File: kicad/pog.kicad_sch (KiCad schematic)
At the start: 179 parts, among them P1 USB_C_Plug_USB2.0, U1 ATmega32U4-A

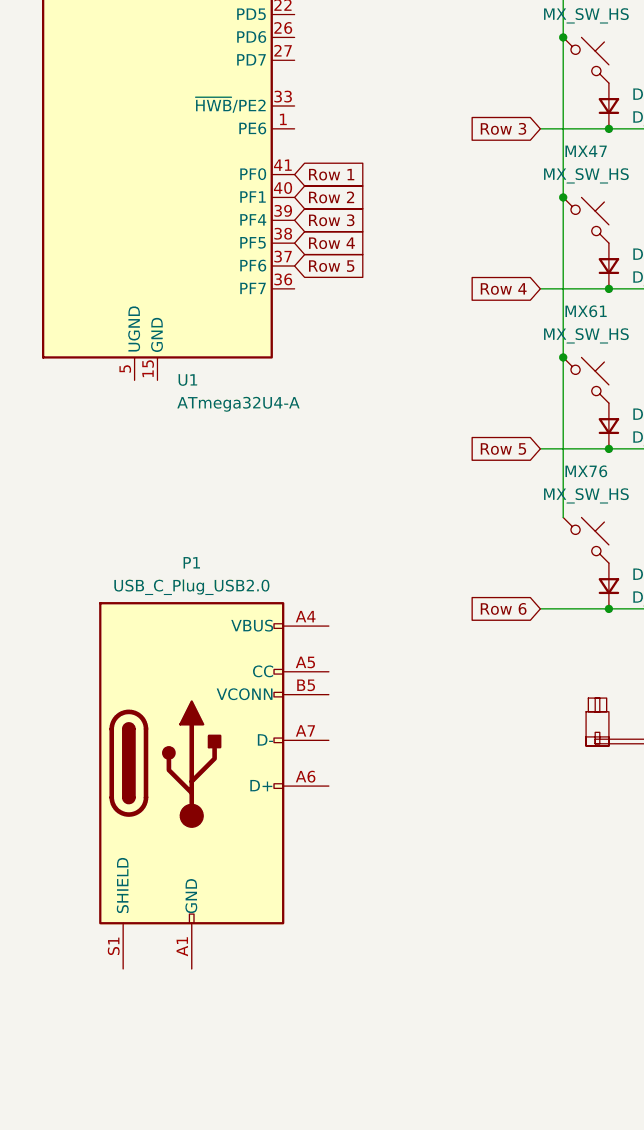
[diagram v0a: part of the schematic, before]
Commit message: more traces and git ignore update
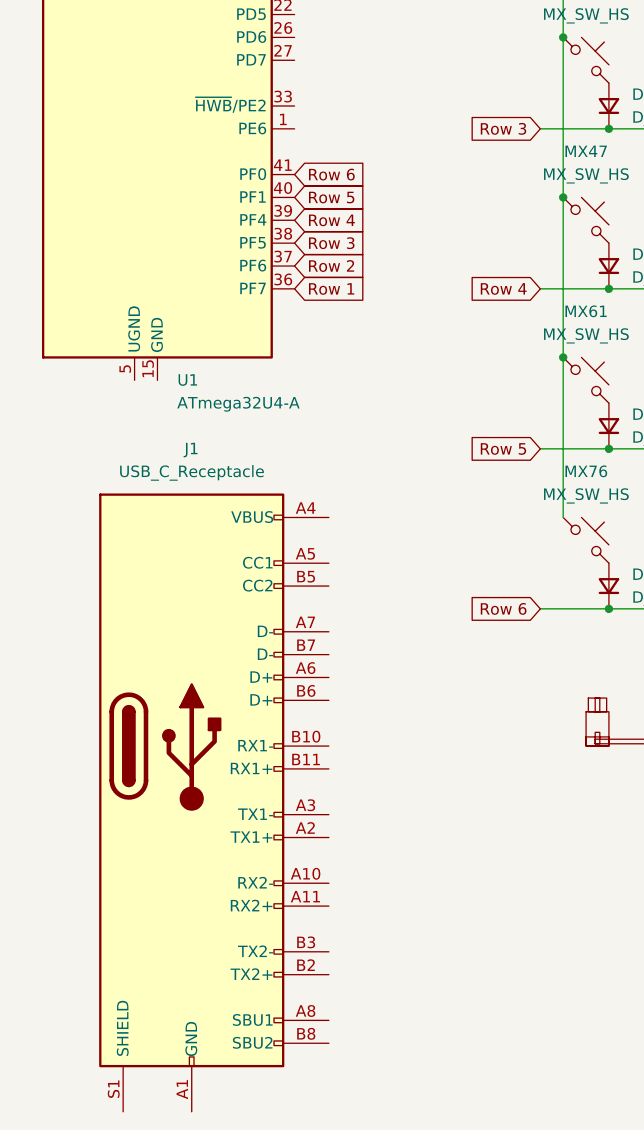
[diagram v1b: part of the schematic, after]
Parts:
- removed P1: USB_C_Plug_USB2.0, Connector_USB:USB_C_Receptacle_HRO_TYPE-C-31-M-12, symbol Connector:USB_C_Plug_USB2.0
- added J1: USB_C_Receptacle, symbol Connector:USB_C_Receptacle
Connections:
- net Row 1: now also U1.36 (PF7); no longer U1.41 (PF0)
- net Row 2: now also U1.37 (PF6); no longer U1.40 (PF1)
- net Row 3: now also U1.38 (PF5); no longer U1.39 (PF4)
- net Row 4: now also U1.39 (PF4); no longer U1.38 (PF5)
- net Row 5: now also U1.40 (PF1); no longer U1.37 (PF6)
- net Row 6: now also U1.41 (PF0)
- new net: J1.A1 (GND), J1.A12 (GND), J1.B1 (GND), J1.B12 (GND)
- new net: J1.A4 (VBUS), J1.A9 (VBUS), J1.B4 (VBUS), J1.B9 (VBUS)
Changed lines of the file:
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@@
     )
   )
-  (global_label "Row 2" (shape input) (at 48.895 87.63 0) (fields_autoplaced)
+  (global_label "Row 2" (shape input) (at 48.895 95.25 0) (fields_autoplaced)
     (effects (font (size 1.27 1.27)) (justify left))
-    (property "Intersheetrefs" "${INTERSHEET_REFS}" (at 57.8068 87.63 0)
+    (property "Intersheetrefs" "${INTERSHEET_REFS}" (at 57.8068 95.25 0)
       (effects (font (size 1.27 1.27)) (justify left) hide)
     )
@@
     )
   )
-  (global_label "Row 5" (shape input) (at 48.895 95.25 0) (fields_autoplaced)
+  (global_label "Row 5" (shape input) (at 48.895 87.63 0) (fields_autoplaced)
     (effects (font (size 1.27 1.27)) (justify left))
-    (property "Intersheetrefs" "${INTERSHEET_REFS}" (at 57.8068 95.25 0)
+    (property "Intersheetrefs" "${INTERSHEET_REFS}" (at 57.8068 87.63 0)
       (effects (font (size 1.27 1.27)) (justify left) hide)
     )
   )
-  (global_label "Row 4" (shape input) (at 48.895 92.71 0) (fields_autoplaced)
+  (global_label "Row 4" (shape input) (at 48.895 90.17 0) (fields_autoplaced)
     (effects (font (size 1.27 1.27)) (justify left))
-    (property "Intersheetrefs" "${INTERSHEET_REFS}" (at 57.8068 92.71 0)
+    (property "Intersheetrefs" "${INTERSHEET_REFS}" (at 57.8068 90.17 0)
+      (effects (font (size 1.27 1.27)) (justify left) hide)
+    )
+  )
+  (global_label "Row 6" (shape input) (at 48.895 85.09 0) (fields_autoplaced)
+    (effects (font (size 1.27 1.27)) (justify left))
+    (property "Intersheetrefs" "${INTERSHEET_REFS}" (at 57.8068 85.09 0)
       (effects (font (size 1.27 1.27)) (justify left) hide)
     )
@@
     )
   )
-  (global_label "Row 1" (shape input) (at 48.895 85.09 0) (fields_autoplaced)
+  (global_label "Row 1" (shape input) (at 48.895 97.79 0) (fields_autoplaced)
     (effects (font (size 1.27 1.27)) (justify left))
-    (property "Intersheetrefs" "${INTERSHEET_REFS}" (at 57.8068 85.09 0)
+    (property "Intersheetrefs" "${INTERSHEET_REFS}" (at 57.8068 97.79 0)
       (effects (font (size 1.27 1.27)) (justify left) hide)
     )
@@
     )
   )
-  (global_label "Row 3" (shape input) (at 48.895 90.17 0) (fields_autoplaced)
+  (global_label "Row 3" (shape input) (at 48.895 92.71 0) (fields_autoplaced)
     (effects (font (size 1.27 1.27)) (justify left))
-    (property "Intersheetrefs" "${INTERSHEET_REFS}" (at 57.8068 90.17 0)
+    (property "Intersheetrefs" "${INTERSHEET_REFS}" (at 57.8068 92.71 0)
       (effects (font (size 1.27 1.27)) (justify left) hide)
     )
@@
     )
   )
-  (symbol (lib_id "Connector:USB_C_Plug_USB2.0") (at 37.465 150.495 0) (unit 1)
-    (in_bom yes) (on_board yes) (dnp no) (fields_autoplaced)
-    (property "Reference" "P1" (at 37.465 128.27 0)
-      (effects (font (size 1.27 1.27)))
-    )
-    (property "Value" "USB_C_Plug_USB2.0" (at 37.465 130.81 0)
-      (effects (font (size 1.27 1.27)))
-    )
-    (property "Footprint" "Connector_USB:USB_C_Receptacle_HRO_TYPE-C-31-M-12" (at 41.275 150.495 0)
-      (effects (font (size 1.27 1.27)) hide)
-    )
-    (property "Datasheet" "https://www.usb.org/sites/default/files/documents/usb_type-c.zip" (at 41.275 150.495 0)
-      (effects (font (size 1.27 1.27)) hide)
-    )
-    (pin "A1")
-    (pin "A12")
-    (pin "A4")
-    (pin "A5")
-    (pin "A6")
-    (pin "A7")
-    (pin "A9")
-    (pin "B1")
-    (pin "B12")
-    (pin "B4")
-    (pin "B5")
-    (pin "B9")
-    (pin "S1")
-    (instances
-      (project "pog"
-        (path "/0904c928-be14-4e09-9349-b8c6153656fb"
-          (reference "P1") (unit 1)
-        )
-      )
-    )
-  )
   (symbol (lib_id "PCM_marbastlib-mx:MX_SW_HS") (at 218.44 72.39 0) (unit 1)
     (in_bom yes) (on_board yes) (dnp no) (fields_autoplaced)
@@
         )
       )
+    )
+  )
+  (symbol (lib_id "Connector:USB_C_Receptacle") (at 37.465 148.59 0) (unit 1)
+    (in_bom yes) (on_board yes) (dnp no) (fields_autoplaced)
+    (property "Reference" "J1" (at 37.465 115.57 0)
+      (effects (font (size 1.27 1.27)))
+    )
+    (property "Value" "USB_C_Receptacle" (at 37.465 118.11 0)
+      (effects (font (size 1.27 1.27)))
+    )
+    (property "Footprint" "" (at 41.275 148.59 0)
+      (effects (font (size 1.27 1.27)) hide)
+    )
+    (property "Datasheet" "https://www.usb.org/sites/default/files/documents/usb_type-c.zip" (at 41.275 148.59 0)
+      (effects (font (size 1.27 1.27)) hide)
+    )
+    (pin "A1")
+    (pin "A10")
+    (pin "A11")
+    (pin "A12")
+    (pin "A2")
+    (pin "A3")
+    (pin "A4")
+    (pin "A5")
+    (pin "A6")
+    (pin "A7")
+    (pin "A8")
+    (pin "A9")
+    (pin "B1")
+    (pin "B10")
+    (pin "B11")
+    (pin "B12")
+    (pin "B2")
+    (pin "B3")
+    (pin "B4")
+    (pin "B5")
+    (pin "B6")
+    (pin "B7")
+    (pin "B8")
+    (pin "B9")
+    (pin "S1")
+    (instances
+      (project "pog"
+        (path "/0904c928-be14-4e09-9349-b8c6153656fb"
+          (reference "J1") (unit 1)
+        )
+      )

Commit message: schematic done
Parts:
- added C1: 1u, Capacitor_SMD:C_1206_3216Metric, symbol Device:C_Small
- added Ground1, Reset1: TestPoint, TestPoint:TestPoint_THTPad_2.0x2.0mm_Drill1.0mm, symbol Connector:TestPoint
- added R1, R2: R, Resistor_SMD:R_1206_3216Metric, symbol Device:R
- added R3, R4: 5.1k, Resistor_SMD:R_1206_3216Metric, symbol Device:R_Small
- added R5, R6: 10k, Resistor_SMD:R_1206_3216Metric, symbol Device:R_Small
- J1: footprint (none) -> USB_C:USB_C_Receptacle_HRO_TYPE-C-31-M-12
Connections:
- net Row 6: now also U1.22 (PD5); no longer U1.41 (PF0)
- net Column 3: now reaches MX19.1, MX3.1, MX34.1, MX49.1, MX63.1, MX78.1
- net Column 3: now also U1.28 (PB4)
- net Column 6: now reaches MX22.1, MX37.1, MX52.1, MX6.1, MX66.1
- net Column 6: now also U1.32 (PC7); no longer MX81.1
- net Column 2: now reaches MX18.1, MX2.1, MX33.1, MX48.1, MX62.1, MX77.1
- net Column 2: now also U1.27 (PD7)
- net Column 16: now reaches MX31.1, MX46.1, MX60.1, MX75.1, MX87.1
- net Column 16: now also MX16.1, U1.20 (PD2); no longer MX15.1
- net Column 15: now reaches MX30.1, MX45.1, MX74.1, MX86.1
- net Column 15: now also MX15.1, U1.19 (PD1); no longer MX14.1
- net Column 12: now reaches MX12.1, MX28.1, MX43.1, MX58.1, MX72.1
- net Column 12: now also MX83.1, U1.10 (PB2)
- net Column 10: now reaches MX10.1, MX26.1, MX41.1, MX56.1, MX70.1
- net Column 10: now also MX81.1, U1.8 (PB0); no longer MX85.1
- net Column 7: now reaches MX23.1, MX38.1, MX53.1, MX67.1, MX7.1
- net Column 7: now also MX80.1, U1.30 (PB6); no longer MX82.1
- net Column 9: now reaches MX25.1, MX40.1, MX55.1, MX69.1, MX9.1
- net Column 9: now also U1.1 (PE6); no longer MX84.1
- net Column 8: now reaches MX24.1, MX39.1, MX54.1, MX68.1, MX8.1
- net Column 8: now also U1.41 (PF0); no longer MX83.1
- net Column 4: now reaches MX20.1, MX35.1, MX4.1, MX50.1, MX64.1, MX79.1
- net Column 4: now also U1.29 (PB5)
- net Column 5: now reaches MX21.1, MX36.1, MX5.1, MX51.1, MX65.1
- net Column 5: now also U1.31 (PC6); no longer MX80.1
- net Column 1: now reaches MX1.1, MX17.1, MX32.1, MX47.1, MX61.1, MX76.1
- net Column 1: now also U1.26 (PD6)
- net Column 13: now reaches MX13.1, MX29.1, MX44.1, MX59.1, MX73.1
- net Column 13: now also MX84.1, U1.11 (PB3)
- net Column 11: now reaches MX11.1, MX27.1, MX42.1, MX57.1, MX71.1
- net Column 11: now also MX82.1, U1.9 (PB1)
- net at U1.13 (~{RESET}): now also R5.2, Reset1.1
- net VCC: now reaches U1.14 (VCC), U1.34 (VCC)
- net VCC: now also J1.A4 (VBUS), J1.A9 (VBUS), J1.B4 (VBUS), J1.B9 (VBUS), U1.2 (UVCC), U1.24 (AVCC), U1.44 (AVCC), U1.7 (VBUS), R5.1
- net GND: now reaches U1.15 (GND), U1.23 (GND), U1.35 (GND), U1.43 (GND)
- net GND: now also J1.A1 (GND), J1.A12 (GND), J1.B1 (GND), J1.B12 (GND), J1.S1 (SHIELD), U1.5 (UGND), C1.1, Ground1.1, R3.1, R4.1, R6.2
- net Column 14: now reaches U1.18 (PD0)
- net Column 14: now also MX14.1, MX85.1
- net at U1.3 (D-): now also R1.1
- net at U1.33 (~{HWB}/PE2): now also R6.1
- net at U1.4 (D+): now also R2.1
- net at U1.6 (UCAP): now also C1.2
- net at J1.A5 (CC1): now also R3.2
- net at J1.A6 (D+): now also J1.B6 (D+), R2.2
- net at J1.A7 (D-): now also J1.B7 (D-), R1.2
- net at J1.B5 (CC2): now also R4.2
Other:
- moved on the sheet: D1, D10, D11, D12, D13, D14, D15, D16, D17, D18, D19, D2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

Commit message: complete basic pcb design
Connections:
- net Column 1: now also U1.1 (PE6); no longer U1.26 (PD6)
- net Column 10: now also U1.25 (PD4); no longer U1.8 (PB0)
- net Column 11: now also U1.26 (PD6); no longer U1.9 (PB1)
- net Column 12: now also U1.27 (PD7); no longer U1.10 (PB2)
- net Column 13: now also U1.28 (PB4); no longer U1.11 (PB3)
- net Column 14: now also U1.31 (PC6); no longer U1.18 (PD0)
- net Column 15: now also U1.29 (PB5); no longer U1.19 (PD1)
- net Column 16: now also U1.30 (PB6); no longer U1.20 (PD2)
- net Column 2: now also U1.32 (PC7); no longer U1.27 (PD7)
- net Column 3: now also U1.10 (PB2); no longer U1.28 (PB4)
- net Column 4: now also U1.11 (PB3); no longer U1.29 (PB5)
- net Column 5: now also U1.18 (PD0); no longer U1.31 (PC6)
- net Column 6: now also U1.19 (PD1); no longer U1.32 (PC7)
- net Column 7: now also U1.20 (PD2); no longer U1.30 (PB6)
- net Column 8: now also U1.21 (PD3); no longer U1.41 (PF0)
- net Column 9: now also U1.22 (PD5); no longer U1.1 (PE6)
- net Row 1: now also U1.9 (PB1); no longer U1.36 (PF7)
- net Row 2: now also U1.8 (PB0); no longer U1.37 (PF6)
- net Row 3: now also U1.41 (PF0); no longer U1.38 (PF5)
- net Row 4: now also U1.40 (PF1); no longer U1.39 (PF4)
- net Row 5: now also U1.39 (PF4); no longer U1.40 (PF1)
- net Row 6: now also U1.38 (PF5); no longer U1.22 (PD5)

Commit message: pre switch flip
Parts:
- added H1, H2, H3, H4, H5, H6, H7, H8: MountingHole, MountingHole:MountingHole_2.1mm, symbol Mechanical:MountingHole
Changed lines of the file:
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@@
     )
   )
+  (symbol (lib_id "Mechanical:MountingHole") (at 116.84 168.275 0) (unit 1)
+    (in_bom yes) (on_board yes) (dnp no) (fields_autoplaced)
+    (property "Reference" "H6" (at 119.38 167.005 0)
+      (effects (font (size 1.27 1.27)) (justify left))
+    )
+    (property "Value" "MountingHole" (at 119.38 169.545 0)
+      (effects (font (size 1.27 1.27)) (justify left))
+    )
+    (property "Footprint" "MountingHole:MountingHole_2.1mm" (at 116.84 168.275 0)
+      (effects (font (size 1.27 1.27)) hide)
+    )
+    (property "Datasheet" "~" (at 116.84 168.275 0)
+      (effects (font (size 1.27 1.27)) hide)
+    )
+    (instances
+      (project "pog"
+        (path "/0904c928-be14-4e09-9349-b8c6153656fb"
+          (reference "H6") (unit 1)
+        )
+      )
+    )
+  )
   (symbol (lib_id "Device:D_Small") (at 147.32 62.23 90) (unit 1)
     (in_bom yes) (on_board yes) (dnp no) (fields_autoplaced)
@@
     )
   )
+  (symbol (lib_id "Mechanical:MountingHole") (at 97.79 161.29 0) (unit 1)
+    (in_bom yes) (on_board yes) (dnp no) (fields_autoplaced)
+    (property "Reference" "H1" (at 100.33 160.02 0)
+      (effects (font (size 1.27 1.27)) (justify left))
+    )
+    (property "Value" "MountingHole" (at 100.33 162.56 0)
+      (effects (font (size 1.27 1.27)) (justify left))
+    )
+    (property "Footprint" "MountingHole:MountingHole_2.1mm" (at 97.79 161.29 0)
+      (effects (font (size 1.27 1.27)) hide)
+    )
+    (property "Datasheet" "~" (at 97.79 161.29 0)
+      (effects (font (size 1.27 1.27)) hide)
+    )
+    (instances
+      (project "pog"
+        (path "/0904c928-be14-4e09-9349-b8c6153656fb"
+          (reference "H1") (unit 1)
+        )
+      )
+    )
+  )
   (symbol (lib_id "Device:R") (at 27.94 126.365 0) (unit 1)
     (in_bom yes) (on_board yes) (dnp no) (fields_autoplaced)
@@
     )
   )
+  (symbol (lib_id "Mechanical:MountingHole") (at 135.255 168.275 0) (unit 1)
+    (in_bom yes) (on_board yes) (dnp no) (fields_autoplaced)
+    (property "Reference" "H7" (at 137.795 167.005 0)
+      (effects (font (size 1.27 1.27)) (justify left))
+    )
+    (property "Value" "MountingHole" (at 137.795 169.545 0)
+      (effects (font (size 1.27 1.27)) (justify left))
+    )
+    (property "Footprint" "MountingHole:MountingHole_2.1mm" (at 135.255 168.275 0)
+      (effects (font (size 1.27 1.27)) hide)
+    )
+    (property "Datasheet" "~" (at 135.255 168.275 0)
+      (effects (font (size 1.27 1.27)) hide)
+    )
+    (instances
+      (project "pog"
+        (path "/0904c928-be14-4e09-9349-b8c6153656fb"
+          (reference "H7") (unit 1)
+        )
+      )
+    )
+  )
   (symbol (lib_id "Device:D_Small") (at 158.75 97.79 90) (unit 1)
     (in_bom yes) (on_board yes) (dnp no)
@@
     )
   )
+  (symbol (lib_id "Mechanical:MountingHole") (at 97.79 167.64 0) (unit 1)
+    (in_bom yes) (on_board yes) (dnp no) (fields_autoplaced)
+    (property "Reference" "H5" (at 100.33 166.37 0)
+      (effects (font (size 1.27 1.27)) (justify left))
+    )
+    (property "Value" "MountingHole" (at 100.33 168.91 0)
+      (effects (font (size 1.27 1.27)) (justify left))
+    )
+    (property "Footprint" "MountingHole:MountingHole_2.1mm" (at 97.79 167.64 0)
+      (effects (font (size 1.27 1.27)) hide)
+    )
+    (property "Datasheet" "~" (at 97.79 167.64 0)
+      (effects (font (size 1.27 1.27)) hide)
+    )
+    (instances
+      (project "pog"
+        (path "/0904c928-be14-4e09-9349-b8c6153656fb"
+          (reference "H5") (unit 1)
+        )
+      )
+    )
+  )
   (symbol (lib_id "Connector:TestPoint") (at 22.225 22.225 0) (unit 1)
     (in_bom yes) (on_board yes) (dnp no)
@@
     )
   )
+  (symbol (lib_id "Mechanical:MountingHole") (at 153.67 168.275 0) (unit 1)
+    (in_bom yes) (on_board yes) (dnp no) (fields_autoplaced)
+    (property "Reference" "H8" (at 156.21 167.005 0)
+      (effects (font (size 1.27 1.27)) (justify left))
+    )
+    (property "Value" "MountingHole" (at 156.21 169.545 0)
+      (effects (font (size 1.27 1.27)) (justify left))
+    )
+    (property "Footprint" "MountingHole:MountingHole_2.1mm" (at 153.67 168.275 0)
+      (effects (font (size 1.27 1.27)) hide)
+    )
+    (property "Datasheet" "~" (at 153.67 168.275 0)
+      (effects (font (size 1.27 1.27)) hide)
+    )
+    (instances
+      (project "pog"
+        (path "/0904c928-be14-4e09-9349-b8c6153656fb"
+          (reference "H8") (unit 1)
+        )
+      )
+    )
+  )
   (symbol (lib_id "power:GND") (at 78.105 84.455 90) (unit 1)
     (in_bom yes) (on_board yes) (dnp no)
@@
     )
   )
+  (symbol (lib_id "Mechanical:MountingHole") (at 116.84 161.29 0) (unit 1)
+    (in_bom yes) (on_board yes) (dnp no) (fields_autoplaced)
+    (property "Reference" "H2" (at 119.38 160.02 0)
+      (effects (font (size 1.27 1.27)) (justify left))
+    )
+    (property "Value" "MountingHole" (at 119.38 162.56 0)
+      (effects (font (size 1.27 1.27)) (justify left))
+    )
+    (property "Footprint" "MountingHole:MountingHole_2.1mm" (at 116.84 161.29 0)
+      (effects (font (size 1.27 1.27)) hide)
+    )
+    (property "Datasheet" "~" (at 116.84 161.29 0)
+      (effects (font (size 1.27 1.27)) hide)
+    )
+    (instances
+      (project "pog"
+        (path "/0904c928-be14-4e09-9349-b8c6153656fb"
+          (reference "H2") (unit 1)
+        )
+      )
+    )
+  )
   (symbol (lib_id "PCM_marbastlib-mx:MX_SW_HS") (at 179.07 92.71 0) (unit 1)
     (in_bom yes) (on_board yes) (dnp no) (fields_autoplaced)
@@
     )
   )
+  (symbol (lib_id "Mechanical:MountingHole") (at 153.67 161.29 0) (unit 1)
+    (in_bom yes) (on_board yes) (dnp no) (fields_autoplaced)
+    (property "Reference" "H4" (at 156.21 160.02 0)
+      (effects (font (size 1.27 1.27)) (justify left))
+    )
+    (property "Value" "MountingHole" (at 156.21 162.56 0)
+      (effects (font (size 1.27 1.27)) (justify left))
+    )
+    (property "Footprint" "MountingHole:MountingHole_2.1mm" (at 153.67 161.29 0)
+      (effects (font (size 1.27 1.27)) hide)
+    )
+    (property "Datasheet" "~" (at 153.67 161.29 0)
+      (effects (font (size 1.27 1.27)) hide)
+    )
+    (instances
+      (project "pog"
+        (path "/0904c928-be14-4e09-9349-b8c6153656fb"
+          (reference "H4") (unit 1)
+        )
+      )
+    )
+  )
   (symbol (lib_id "PCM_marbastlib-mx:MX_SW_HS") (at 213.36 39.37 0) (unit 1)
     (in_bom yes) (on_board yes) (dnp no) (fields_autoplaced)
@@
         )
       )
+    )
+  )
+  (symbol (lib_id "Mechanical:MountingHole") (at 135.255 161.29 0) (unit 1)
+    (in_bom yes) (on_board yes) (dnp no) (fields_autoplaced)
+    (property "Reference" "H3" (at 137.795 160.02 0)
+      (effects (font (size 1.27 1.27)) (justify left))
+    )
+    (property "Value" "MountingHole" (at 137.795 162.56 0)
+      (effects (font (size 1.27 1.27)) (justify left))
+    )
+    (property "Footprint" "MountingHole:MountingHole_2.1mm" (at 135.255 161.29 0)
+      (effects (font (size 1.27 1.27)) hide)
+    )
+    (property "Datasheet" "~" (at 135.255 161.29 0)
+      (effects (font (size 1.27 1.27)) hide)
+    )
+    (instances
+      (project "pog"
+        (path "/0904c928-be14-4e09-9349-b8c6153656fb"
+          (reference "H3") (unit 1)
+        )
+      )

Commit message: switch to pcb mount stabilizers
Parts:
- S1: footprint PCM_marbastlib-mx:STAB_MX_P_2u -> PCM_marbastlib-mx:STAB_MX_2u
- S2: footprint PCM_marbastlib-mx:STAB_MX_P_ISO -> PCM_marbastlib-mx:STAB_MX_ISO
- S3: footprint PCM_marbastlib-mx:STAB_MX_P_4.5u -> PCM_marbastlib-mx:STAB_MX_4.5u
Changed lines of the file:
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@@
       (effects (font (size 1.27 1.27)) (justify left))
     )
-    (property "Footprint" "PCM_marbastlib-mx:STAB_MX_P_4.5u" (at 147.32 148.59 0)
+    (property "Footprint" "PCM_marbastlib-mx:STAB_MX_4.5u" (at 147.32 148.59 0)
       (effects (font (size 1.27 1.27)) hide)
     )
@@
       (effects (font (size 1.27 1.27)) (justify left))
     )
-    (property "Footprint" "PCM_marbastlib-mx:STAB_MX_P_ISO" (at 124.46 148.59 0)
+    (property "Footprint" "PCM_marbastlib-mx:STAB_MX_ISO" (at 124.46 148.59 0)
       (effects (font (size 1.27 1.27)) hide)
     )
@@
       (effects (font (size 1.27 1.27)) (justify left))
     )
-    (property "Footprint" "PCM_marbastlib-mx:STAB_MX_P_2u" (at 104.14 148.59 0)
-      (effects (font (size 1.27 1.27)) hide)
-    )
+    (property "Footprint" "PCM_marbastlib-mx:STAB_MX_2u" (at 104.14 148.59 0)
+      (effects (font (size 1.27 1.27)) hide)
+    )
